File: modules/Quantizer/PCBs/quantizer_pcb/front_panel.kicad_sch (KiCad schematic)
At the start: 54 parts, among them J1 THONKICONN, J10 Conn_01x12_Socket, J2 THONKICONN, J3 THONKICONN, J4 THONKICONN, J5 THONKICONN, J6 THONKICONN, J7 THONKICONN, J8 THONKICONN, J9 Conn_01x12_Socket, SW1 TL1105SPF250Q, SW10 TL1105SPF250Q, SW11 TL1105SPF250Q, SW12 TL1105SPF250Q, SW13 TL1105SPF250Q, SW14 TL1105SPF250Q, SW15 TL1105SPF250Q, SW2 TL1105SPF250Q, SW3 TL1105SPF250Q, SW4 TL1105SPF250Q, SW5 TL1105SPF250Q, SW6 TL1105SPF250Q, SW7 TL1105SPF250Q, SW8 TL1105SPF250Q, SW9 TL1105SPF250Q

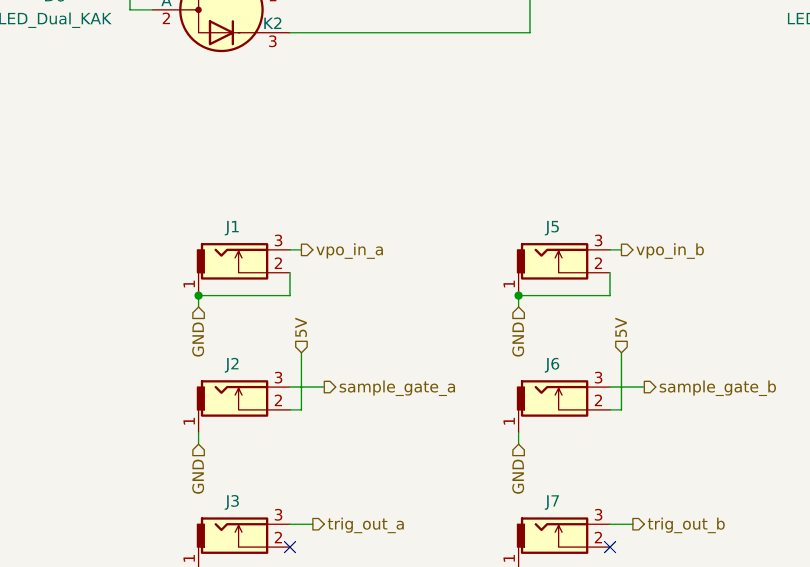
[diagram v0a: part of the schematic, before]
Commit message: Switch to non-inverting op-amp output
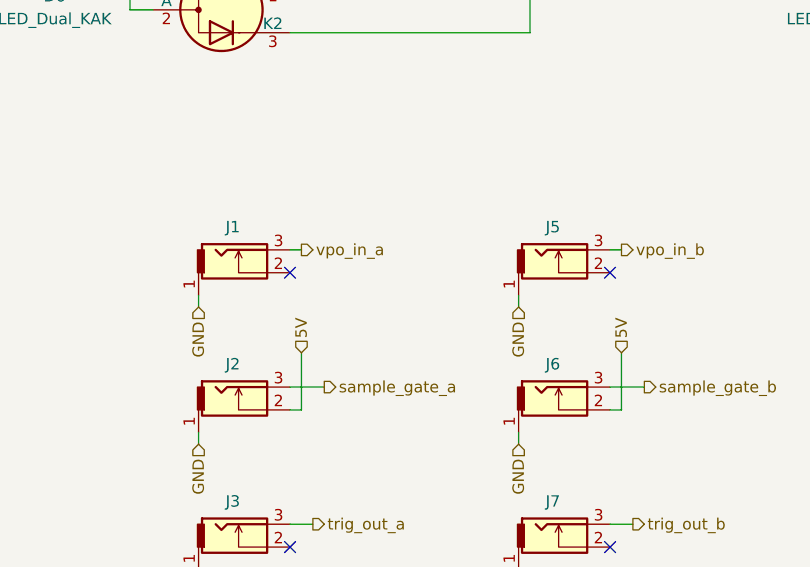
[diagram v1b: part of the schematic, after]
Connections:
- net GND: no longer J1.2, J5.2
- no-connect marks 8 -> 10
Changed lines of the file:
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@@
-	)
-	(junction
-		(at 127 121.92)
-		(diameter 0)
-		(color 0 0 0 0)
 	)
 	(junction
@@
 	(junction
 		(at 83.82 67.31)
-		(diameter 0)
-		(color 0 0 0 0)
-	)
-	(junction
-		(at 91.44 121.92)
 		(diameter 0)
 		(color 0 0 0 0)
@@
 	)
 	(no_connect
+		(at 101.6 119.38)
+	)
+	(no_connect
 		(at 101.6 149.86)
 	)
@@
 		(at 214.63 128.27)
 	)
+	(no_connect
+		(at 137.16 119.38)
+	)
 	(wire
 		(pts
@@
 	(wire
 		(pts
-			(xy 137.16 119.38) (xy 137.16 121.92)
-		)
-		(stroke
-			(width 0)
-			(type default)
-		)
-	)
-	(wire
-		(pts
 			(xy 63.5 34.29) (xy 49.53 34.29)
 		)
@@
 	(wire
 		(pts
-			(xy 137.16 121.92) (xy 127 121.92)
-		)
-		(stroke
-			(width 0)
-			(type default)
-		)
-	)
-	(wire
-		(pts
 			(xy 29.21 125.73) (xy 29.21 135.89)
 		)
@@
 	(wire
 		(pts
-			(xy 101.6 121.92) (xy 91.44 121.92)
-		)
-		(stroke
-			(width 0)
-			(type default)
-		)
-	)
-	(wire
-		(pts
 			(xy 29.21 95.25) (xy 29.21 105.41)
 		)
@@
 		)
 		(stroke
-			(width 0)
-			(type default)
-		)
-	)
-	(wire
-		(pts
-			(xy 101.6 119.38) (xy 101.6 121.92)
-		)
-		(stroke

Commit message: Update quant PCB to v0.2
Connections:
- net 5V: no longer R1.1
- new net vref_+5: R1.1
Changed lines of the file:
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@@
 	(title_block
 		(title "Quantizer")
-		(date "2024-12-18")
-		(rev "v0.1")
+		(date "2025-04-02")
+		(rev "v0.2")
 		(company "Free Modular")
 	)
@@
 		)
 	)
+	(hierarchical_label "vref_+5"
+		(shape input)
+		(at 49.53 21.59 90)
+		(effects
+			(font
+				(size 1.27 1.27)
+			)
+			(justify left)
+		)
+	)
 	(hierarchical_label "GND"
 		(shape input)
@@
 		(effects
 			(font
-				(size 1.27 1.27)
-			)
-			(justify left)
-		)
-	)
-	(hierarchical_label "5V"
-		(shape input)
-		(at 49.53 21.59 90)
-		(effects
-			(font

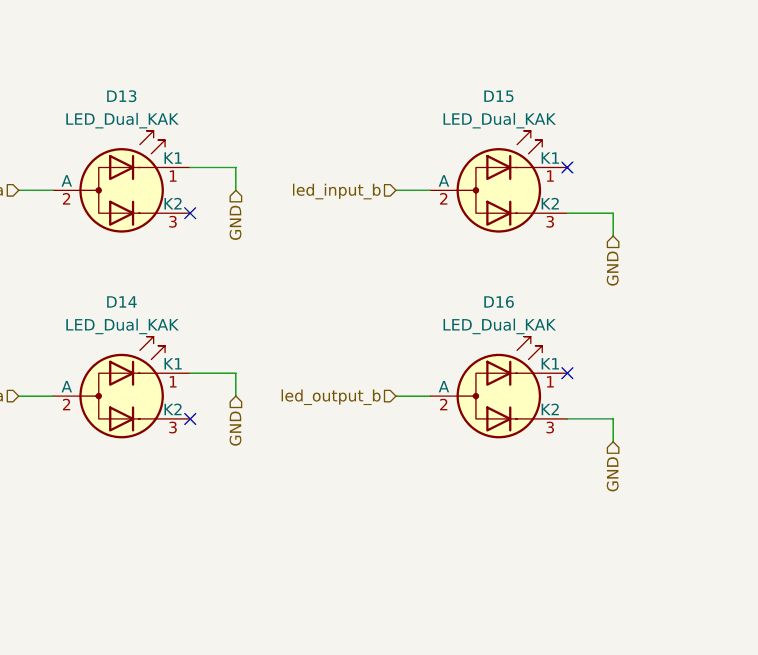
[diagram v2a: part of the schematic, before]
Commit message: Implement trigger outputs
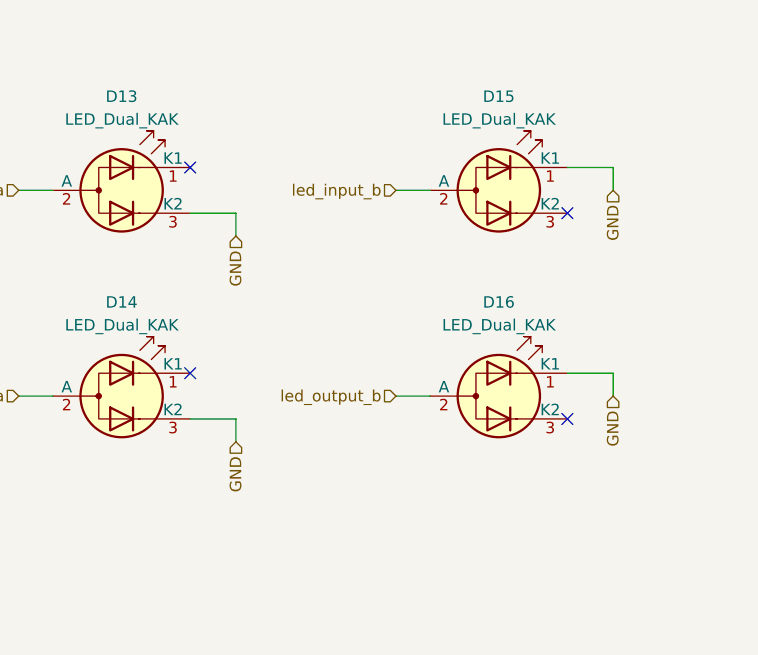
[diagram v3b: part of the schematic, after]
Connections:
- net GND: now also D13.3 (K2), D14.3 (K2), D15.1 (K1), D16.1 (K1); no longer D13.1 (K1), D14.1 (K1), D15.3 (K2), D16.3 (K2)
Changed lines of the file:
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@@
-	)
-	(no_connect
-		(at 256.54 123.19)
 	)
 	(no_connect
@@
 	)
 	(no_connect
-		(at 214.63 151.13)
+		(at 256.54 151.13)
+	)
+	(no_connect
+		(at 256.54 128.27)
 	)
 	(no_connect
@@
 	)
 	(no_connect
+		(at 214.63 146.05)
+	)
+	(no_connect
 		(at 101.6 149.86)
 	)
 	(no_connect
-		(at 256.54 146.05)
-	)
-	(no_connect
-		(at 214.63 128.27)
+		(at 214.63 123.19)
 	)
 	(no_connect
@@
 	(wire
 		(pts
-			(xy 214.63 123.19) (xy 219.71 123.19)
+			(xy 214.63 128.27) (xy 219.71 128.27)
 		)
 		(stroke
@@
 	(wire
 		(pts
-			(xy 219.71 146.05) (xy 219.71 148.59)
+			(xy 219.71 151.13) (xy 219.71 153.67)
 		)
 		(stroke
@@
 	(wire
 		(pts
-			(xy 256.54 151.13) (xy 261.62 151.13)
+			(xy 256.54 146.05) (xy 261.62 146.05)
 		)
 		(stroke
@@
 	(wire
 		(pts
-			(xy 261.62 151.13) (xy 261.62 153.67)
+			(xy 261.62 146.05) (xy 261.62 148.59)
 		)
 		(stroke
@@
 	(wire
 		(pts
-			(xy 214.63 146.05) (xy 219.71 146.05)
+			(xy 214.63 151.13) (xy 219.71 151.13)
 		)
 		(stroke
@@
 	(wire
 		(pts
-			(xy 219.71 123.19) (xy 219.71 125.73)
+			(xy 219.71 128.27) (xy 219.71 130.81)
 		)
 		(stroke
@@
 	(wire
 		(pts
-			(xy 261.62 128.27) (xy 261.62 130.81)
+			(xy 261.62 123.19) (xy 261.62 125.73)
 		)
 		(stroke
@@
 	(wire
 		(pts
-			(xy 256.54 128.27) (xy 261.62 128.27)
+			(xy 256.54 123.19) (xy 261.62 123.19)
 		)
 		(stroke
@@
 	(hierarchical_label "GND"
 		(shape input)
-		(at 261.62 130.81 270)
+		(at 261.62 125.73 270)
 		(effects
 			(font
@@
 	(hierarchical_label "GND"
 		(shape input)
-		(at 261.62 153.67 270)
+		(at 261.62 148.59 270)
 		(effects
 			(font
@@
 	(hierarchical_label "GND"
 		(shape input)
-		(at 219.71 148.59 270)
+		(at 219.71 153.67 270)
 		(effects
 			(font
@@
 	(hierarchical_label "GND"
 		(shape input)
-		(at 219.71 125.73 270)
-		(effects
-			(font
+		(at 219.71 130.81 270)
+		(effects
+			(font
